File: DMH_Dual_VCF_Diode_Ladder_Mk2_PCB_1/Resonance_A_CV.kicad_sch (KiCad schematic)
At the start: 25 parts, among them J17 Conn_01x10_PinHeader, Q1 BC548, Q2 BC548, U1 TL074

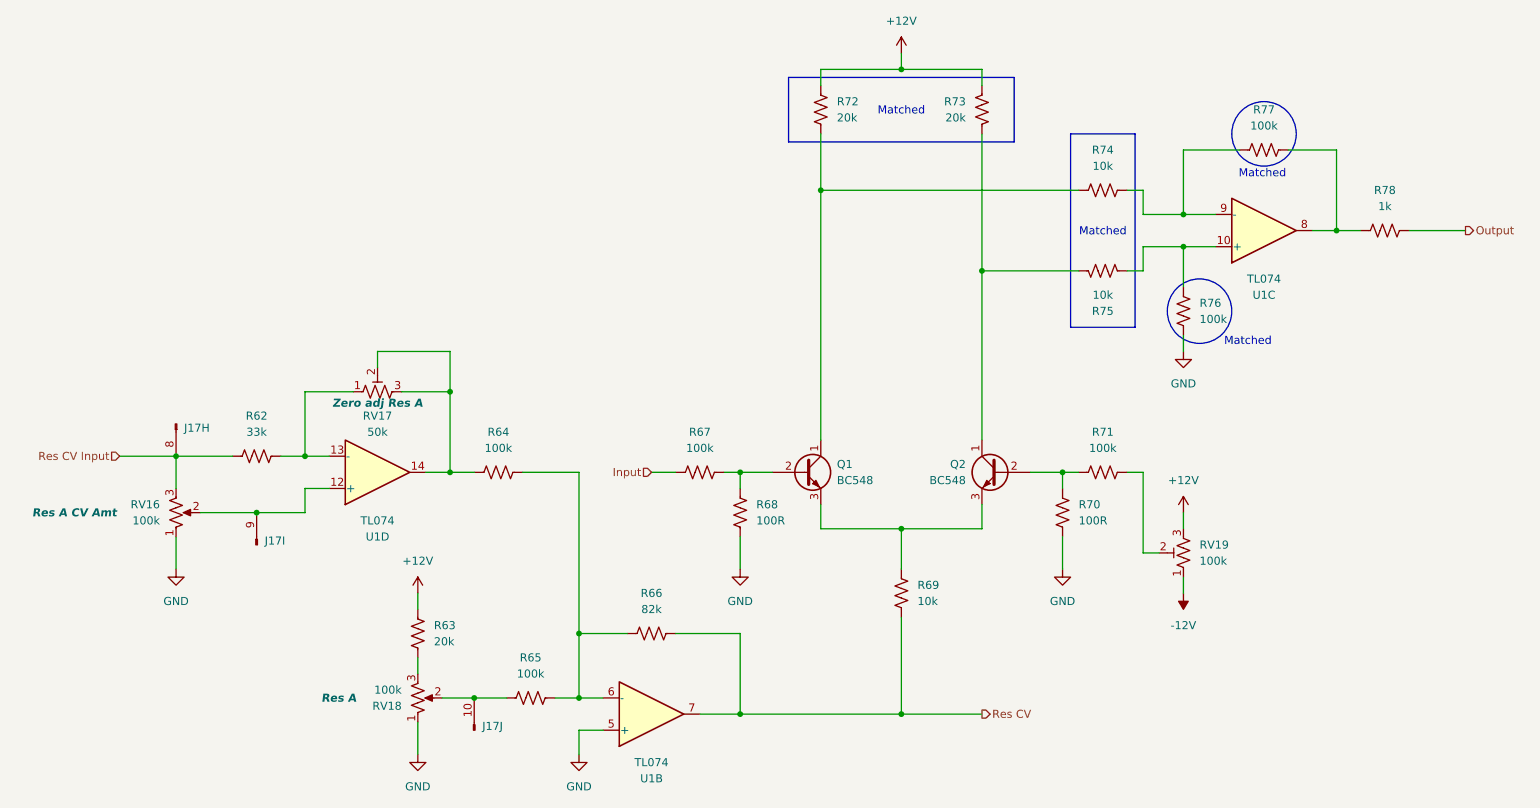
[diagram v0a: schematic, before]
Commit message: Added inter-board pins to all circuits
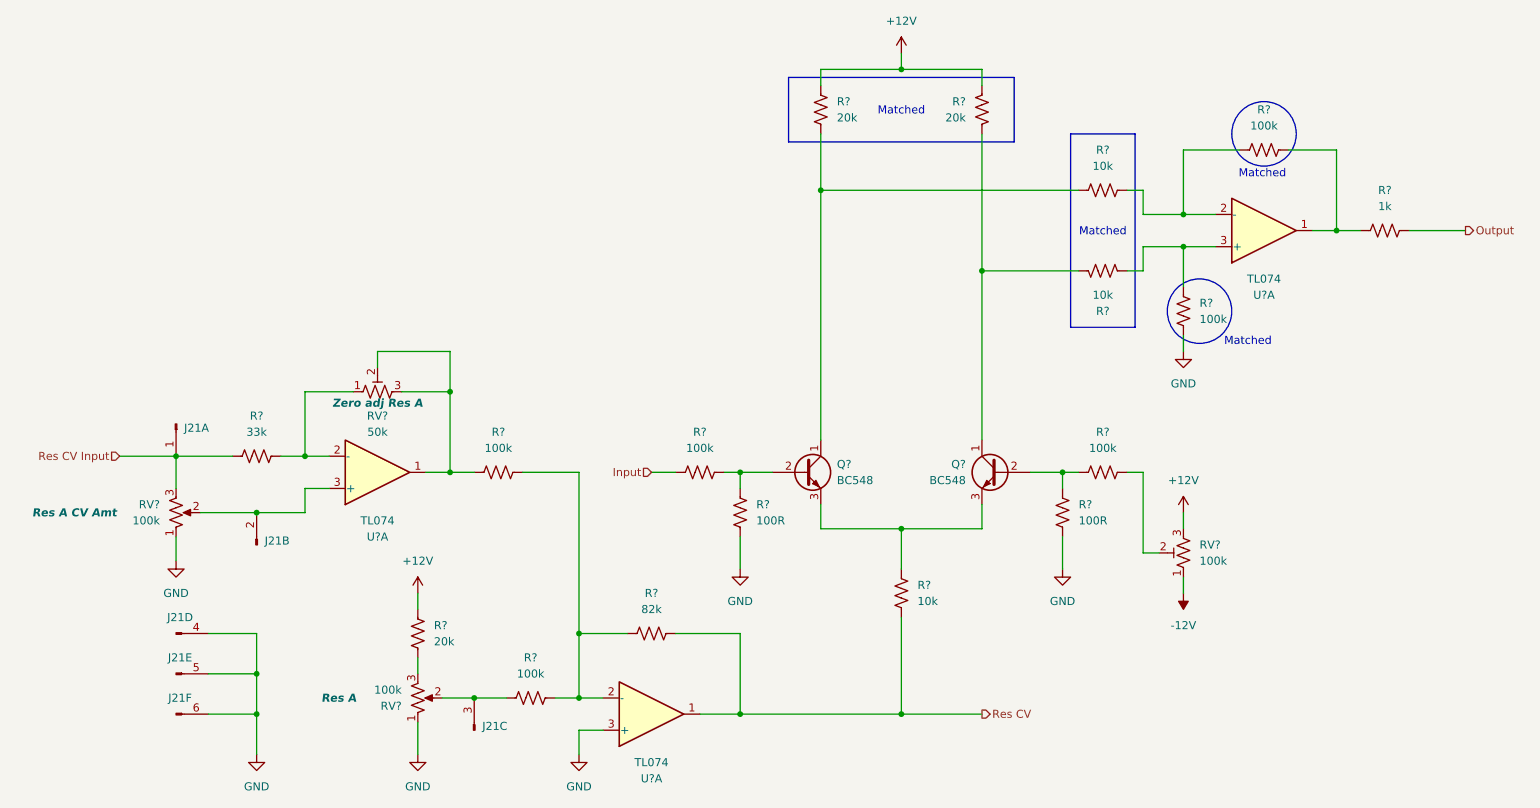
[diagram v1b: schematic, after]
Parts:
- added unit 6 of J21
- added unit 4 of J21
- added unit 5 of J21
- J21: renamed from J17; value Conn_01x10_PinHeader -> Conn_01x06_PinHeader; symbol SynthStuff:Conn_01x10_PinHeader -> SynthStuff:Conn_01x06_PinHeader
- renumbered Q1 to Q?, Q2 to Q?, R66 to R?, R69 to R?, R72 to R?, R65 to R?, R73 to R?, R76 to R?, R78 to R?, R71 to R?, R74 to R?, R62 to R?, R75 to R?, R68 to R?, R64 to R?, R70 to R?, R63 to R?, R77 to R?, R67 to R?, RV17 to RV?, RV19 to RV?, RV16 to RV?, RV18 to RV?, U1 to U?
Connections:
- net GND: now also U?.3 (+), J21.4 (Pin_4), J21.5 (Pin_5), J21.6 (Pin_6); no longer U?.5 (+)
- net Res CV: now also U?.1; no longer U?.7
- net Res CV Input: now also J21.1 (Pin_1); no longer J21.8 (Pin_8)
- net at R?.1, R?.2, R?.2: now also U?.2 (-); no longer U?.6 (-)
- net at R?.2, RV?.1: now also U?.2 (-); no longer U?.13 (-)
- net at R?.1, RV?.2, RV?.3: now also U?.1; no longer U?.14
- net at R?.1, RV?.2: now also J21.3 (Pin_3); no longer J21.10 (Pin_10)
- net at R?.1, R?.1: now also U?.3 (+); no longer U?.10 (+)
- net at R?.1, R?.2: now also U?.1; no longer U?.8
- net at R?.1, R?.2: now also U?.2 (-); no longer U?.9 (-)
- new net: J21.2 (Pin_2), RV?.2, U?.3 (+)

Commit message: Annotating OpAmps in progress
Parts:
- gave numbers to parts that had none: 1
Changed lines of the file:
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@@
 		(on_board yes)
 		(dnp no)
-		(property "Reference" "U?"
+		(property "Reference" "U1"
 			(at 138.43 137.16 0)
 			(effects
@@
 			(project "DMH_Dual_VCF_Diode_Ladder_Mk2_PCB_1"
 				(path "/58f4306d-5387-4983-bb08-41a2313fd315/ad5c5475-8483-41b0-97cc-617422d54799"
-					(reference "U?")
+					(reference "U1")
 					(unit 1)
 				)
@@
 		(on_board yes)
 		(dnp no)
-		(property "Reference" "U?"
+		(property "Reference" "U1"
 			(at 234.95 60.96 0)
 			(effects
@@
 			(project "DMH_Dual_VCF_Diode_Ladder_Mk2_PCB_1"
 				(path "/58f4306d-5387-4983-bb08-41a2313fd315/ad5c5475-8483-41b0-97cc-617422d54799"
-					(reference "U?")
+					(reference "U1")
 					(unit 1)
 				)
@@
 		(on_board yes)
 		(dnp no)
-		(property "Reference" "U?"
+		(property "Reference" "U1"
 			(at 95.25 99.06 0)
 			(effects
@@
 			(project "DMH_Dual_VCF_Diode_Ladder_Mk2_PCB_1"
 				(path "/58f4306d-5387-4983-bb08-41a2313fd315/ad5c5475-8483-41b0-97cc-617422d54799"
-					(reference "U?")
-					(unit 1)
-				)
+					(reference "U1")
+					(unit 1)
+				)

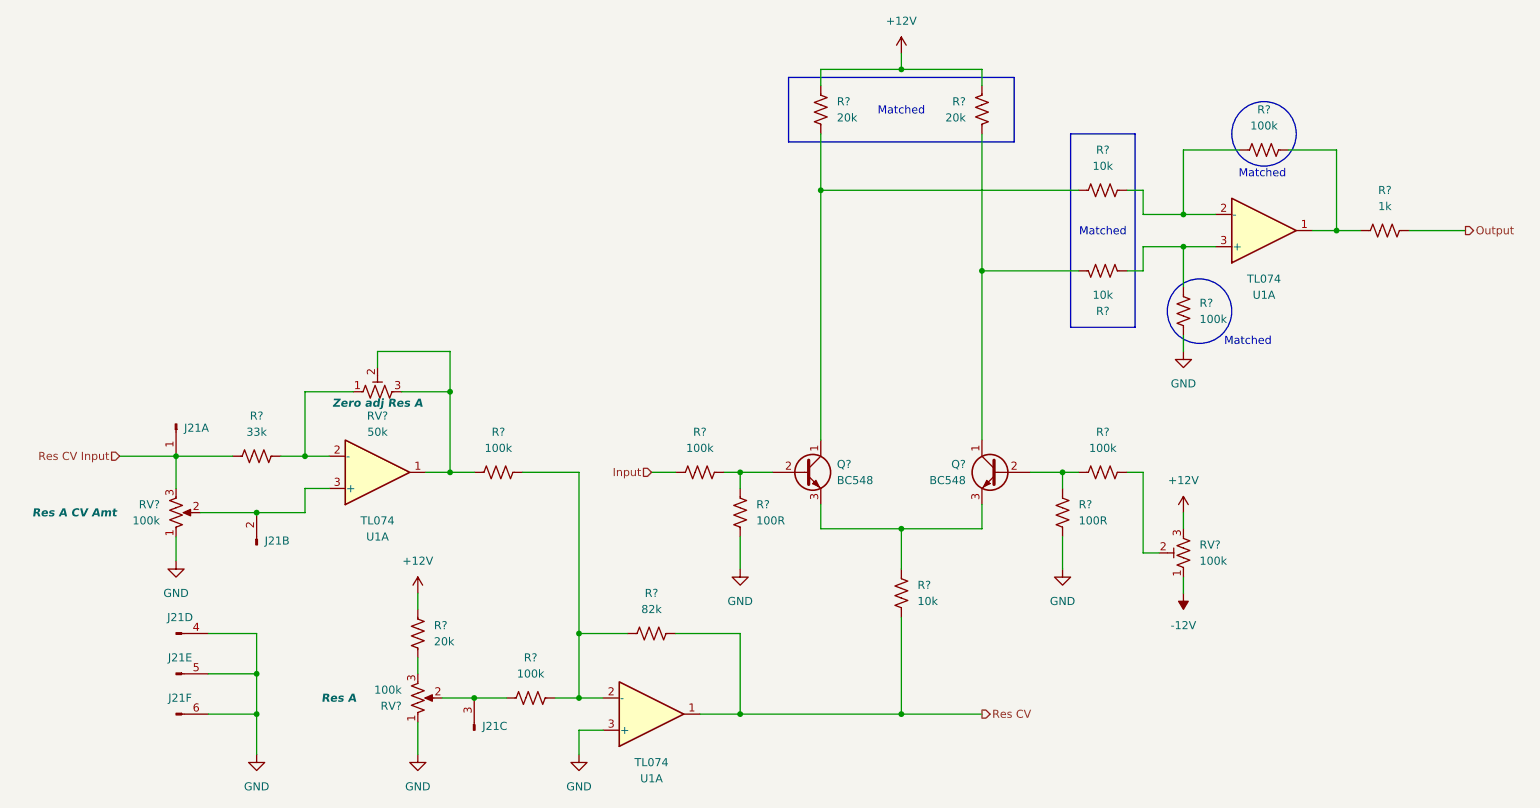
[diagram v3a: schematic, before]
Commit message: Reannotated OpAmps and cleared errors
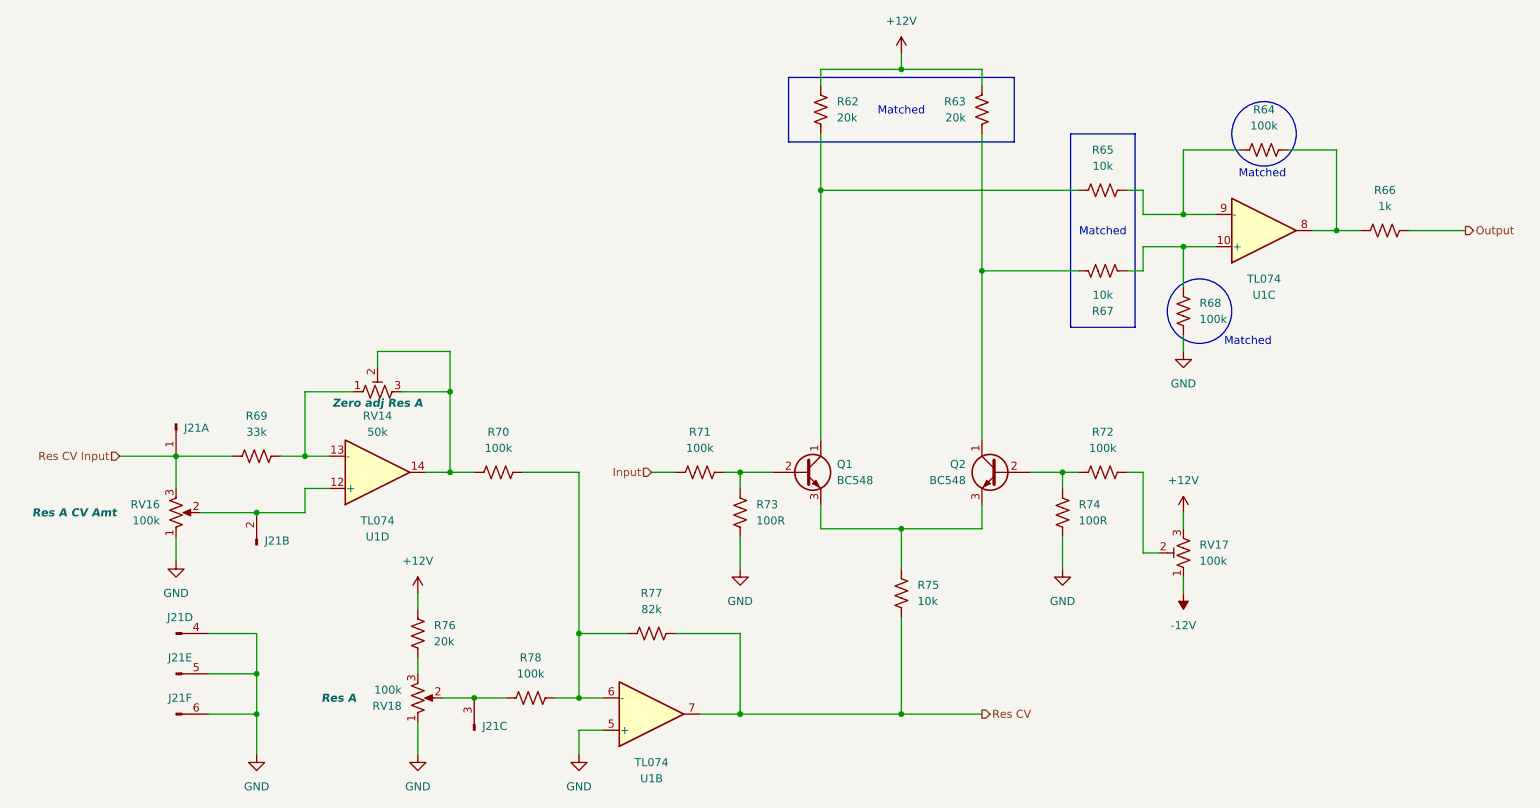
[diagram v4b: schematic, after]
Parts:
- removed Q? (x2): BC548, Package_TO_SOT_THT:TO-92L_Inline_Wide, symbol Transistor_BJT:BC548
- removed R?: 82k, Resistor_THT:R_Axial_DIN0207_L6.3mm_D2.5mm_P7.62mm_Horizontal, symbol Device:R_US
- removed R? (x3): 10k, Resistor_THT:R_Axial_DIN0207_L6.3mm_D2.5mm_P7.62mm_Horizontal, symbol Device:R_US
- removed R? (x3): 20k, Resistor_THT:R_Axial_DIN0207_L6.3mm_D2.5mm_P7.62mm_Horizontal, symbol Device:R_US
- removed R? (x6): 100k, Resistor_THT:R_Axial_DIN0207_L6.3mm_D2.5mm_P7.62mm_Horizontal, symbol Device:R_US
- removed R?: 1k, Resistor_THT:R_Axial_DIN0207_L6.3mm_D2.5mm_P7.62mm_Horizontal, symbol Device:R_US
- removed R?: 33k, Resistor_THT:R_Axial_DIN0207_L6.3mm_D2.5mm_P7.62mm_Horizontal, symbol Device:R_US
- removed R? (x2): 100R, Resistor_THT:R_Axial_DIN0207_L6.3mm_D2.5mm_P7.62mm_Horizontal, symbol Device:R_US
- removed RV?: 50k, Potentiometer_THT:Potentiometer_Bourns_3296W_Vertical, symbol Device:R_Potentiometer_Trim_US
- removed RV?: 100k, Potentiometer_THT:Potentiometer_Bourns_3296W_Vertical, symbol Device:R_Potentiometer_Trim_US
- removed RV?: 100k, SynthStuff:Potentiometer_TT_P110KH1, symbol Device:R_Potentiometer_US
- removed RV?: 100k, SynthStuff:Potentiometer_Alpha_RD901F-40-00D_Single_Vertical, symbol Device:R_Potentiometer_US
- removed U1 (x3): TL074, Package_DIP:DIP-14_W7.62mm_Socket, symbol Amplifier_Operational:TL074
- added Q1, Q2: BC548, Package_TO_SOT_THT:TO-92L_Inline_Wide, symbol Transistor_BJT:BC548
- added R62, R63, R76: 20k, Resistor_THT:R_Axial_DIN0207_L6.3mm_D2.5mm_P7.62mm_Horizontal, symbol Device:R_US
- added R64, R68, R70, R71, R72, R78: 100k, Resistor_THT:R_Axial_DIN0207_L6.3mm_D2.5mm_P7.62mm_Horizontal, symbol Device:R_US
- added R65, R67, R75: 10k, Resistor_THT:R_Axial_DIN0207_L6.3mm_D2.5mm_P7.62mm_Horizontal, symbol Device:R_US
- added R66: 1k, Resistor_THT:R_Axial_DIN0207_L6.3mm_D2.5mm_P7.62mm_Horizontal, symbol Device:R_US
- added R69: 33k, Resistor_THT:R_Axial_DIN0207_L6.3mm_D2.5mm_P7.62mm_Horizontal, symbol Device:R_US
- added R73, R74: 100R, Resistor_THT:R_Axial_DIN0207_L6.3mm_D2.5mm_P7.62mm_Horizontal, symbol Device:R_US
- added R77: 82k, Resistor_THT:R_Axial_DIN0207_L6.3mm_D2.5mm_P7.62mm_Horizontal, symbol Device:R_US
- added RV14: 50k, Potentiometer_THT:Potentiometer_Bourns_3296W_Vertical, symbol Device:R_Potentiometer_Trim_US
- added RV16: 100k, SynthStuff:Potentiometer_TT_P110KH1, symbol Device:R_Potentiometer_US
- added RV17: 100k, Potentiometer_THT:Potentiometer_Bourns_3296W_Vertical, symbol Device:R_Potentiometer_Trim_US
- added RV18: 100k, SynthStuff:Potentiometer_Alpha_RD901F-40-00D_Single_Vertical, symbol Device:R_Potentiometer_US
- added U1: TL074, Package_DIP:DIP-14_W7.62mm_Socket, symbol Amplifier_Operational:TL074
- J21: footprint Connector_PinHeader_2.54mm:PinHeader_1x10_P2.54mm_Vertical -> Connector_PinHeader_2.54mm:PinHeader_1x06_P2.54mm_Vertical
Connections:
- net +12V: now also R62.2, R63.2, R76.2, RV17.3
- net -12V: now also RV17.1
- net GND: now also R68.2, R73.1, R74.1, RV16.1, RV18.1, U1.5 (+)
- net Input: now also R71.2
- net Output: now also R66.1
- net Res CV: now also R75.1, R77.2, U1.7
- net Res CV Input: now also R69.1, RV16.3
- net at J21.3 (Pin_3): now also R78.1, RV18.2
- net at J21.2 (Pin_2): now also RV16.2, U1.12 (+)
- new net: Q1.3 (E), Q2.3 (E), R75.2
- new net: R76.1, RV18.3
- new net: R69.2, RV14.1, U1.13 (-)
- new net: R70.1, RV14.2, RV14.3, U1.14
- new net: R64.2, R65.1, U1.9 (-)
- new net: Q1.1 (C), R62.1, R65.2
- new net: R72.1, RV17.2
- new net: Q1.2 (B), R71.1, R73.2
- new net: R70.2, R77.1, R78.2, U1.6 (-)
- new net: Q2.1 (C), R63.1, R67.2
- new net: R67.1, R68.1, U1.10 (+)
- new net: R64.1, R66.2, U1.8
- new net: Q2.2 (B), R72.2, R74.2
